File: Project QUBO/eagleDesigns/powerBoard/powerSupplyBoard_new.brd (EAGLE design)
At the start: 152.4 x 101.6 mm, 146 parts

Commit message: placed everything preliminarily
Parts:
- C15, C3, C6: value (none) -> 22 uF
- moved R39 268.9 mm to (147.3, 59.7)
- moved R40 268.2 mm to (141.0, 74.9)
- moved R38 261.8 mm to (147.3, 57.1), turned to 180 degrees
- moved R37 253.5 mm to (147.3, 62.2)
- moved REN_H 253.4 mm to (121.9, 27.9)
- moved C_OUT_5V 246.3 mm to (128.3, 7.62)
- moved R36 245.5 mm to (147.3, 64.8), turned to 180 degrees
- moved 5VCS 240.9 mm to (115.6, 36.8), turned to 270 degrees
- moved REN_T 239.0 mm to (114.3, 27.9), turned to 180 degrees
- moved R35 238.2 mm to (148.6, 72.4), turned to 180 degrees
- moved R34 230.3 mm to (148.6, 74.9)
- moved RFBT 224.5 mm to (114.3, 12.7)
- moved RFBB 214.4 mm to (114.3, 17.8)
- moved R47 214.1 mm to (147.3, 45.7)
- moved C_BYP7 205.1 mm to (123.2, 17.8)
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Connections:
- removed net N$59 (its old number): REN_B.1, REN_H.1, REN_T.2, U$5.C
- removed net N$60: R36.1, R37.2
- removed net N$61: ADC.SCL
- removed net N$63: ADC.SDA
- removed net N$75: BAT1HSOR.SHDN, HIGHSIDEMOS1.D, R48.1
- removed net N$76: ADC.CH7, R34.1, R35.2, R38.2
- removed net N$77: ADC.CH8
- removed net N$78: ADC.CH9
- removed net N$79: ADC.CH10
- removed net N$80: ADC.CH11
- removed net N$81: ADC.CH12
- removed net N$82: ADC.CH13
- removed net N$84: IOEXPANDER.23
- removed net N$86: IOEXPANDER.22
- new net N$32: ADC.CH7, R34.1, R35.2
- new net N$55: ADC.CH8, R36.1, R37.2
- net 12V: now also R42.2
- net 16V: now also R40.2
- net 3.3V: now also R46.2
- net 5V: now also R44.2
- net BAT2: now also R18.2
- net BAT3: now also R29.2, R38.2
- net GND: now also BAT1HSOR.SHDN, HIGHSIDEMOS1.D, R48.1, REN_B.1, REN_H.1, REN_T.2, U$5.C
- net N$66: now also ADC.CH9
- net N$71: now also ADC.CH10
- net N$72: now also ADC.CH11
- net N$73: now also ADC.CH12
- net N$74: now also ADC.CH13
- net SCL1: now also ADC.SCL, IOEXPANDER.22
- net SDA1: now also ADC.SDA, IOEXPANDER.23

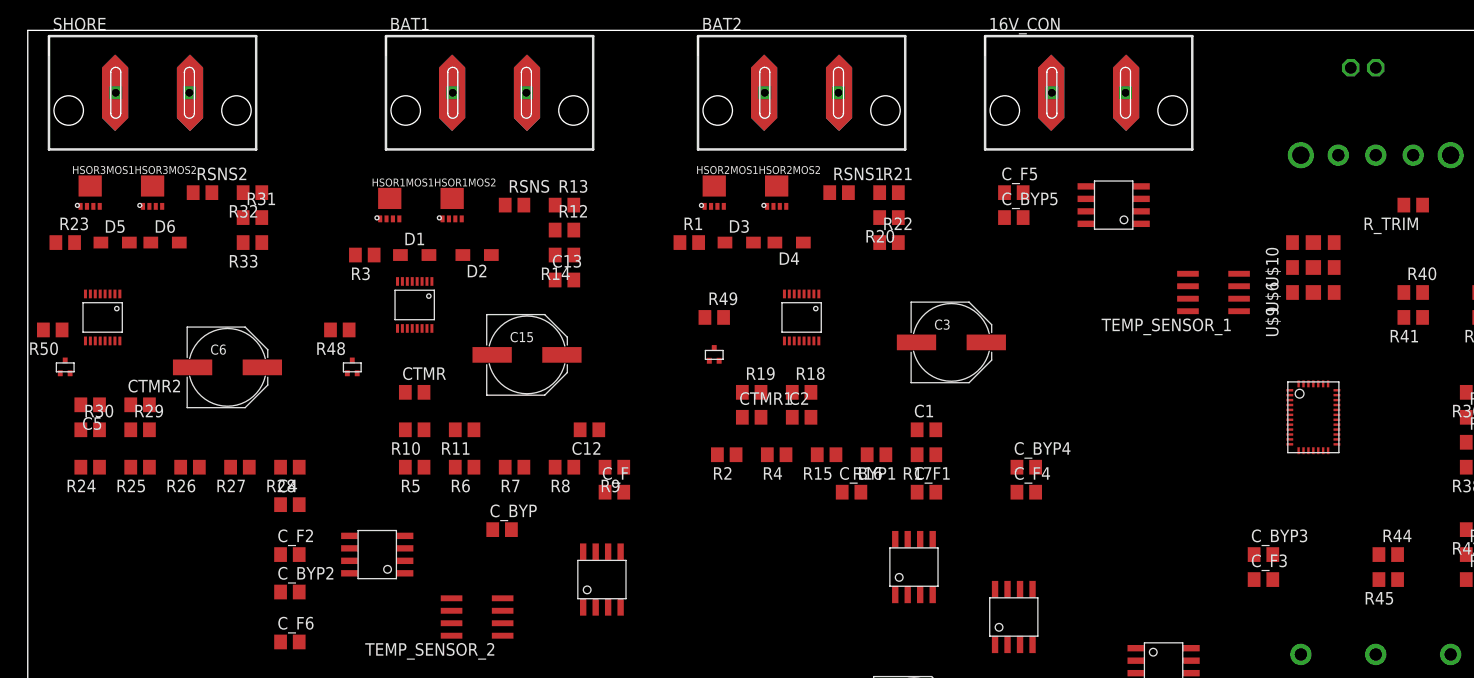
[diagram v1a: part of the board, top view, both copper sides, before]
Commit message: 
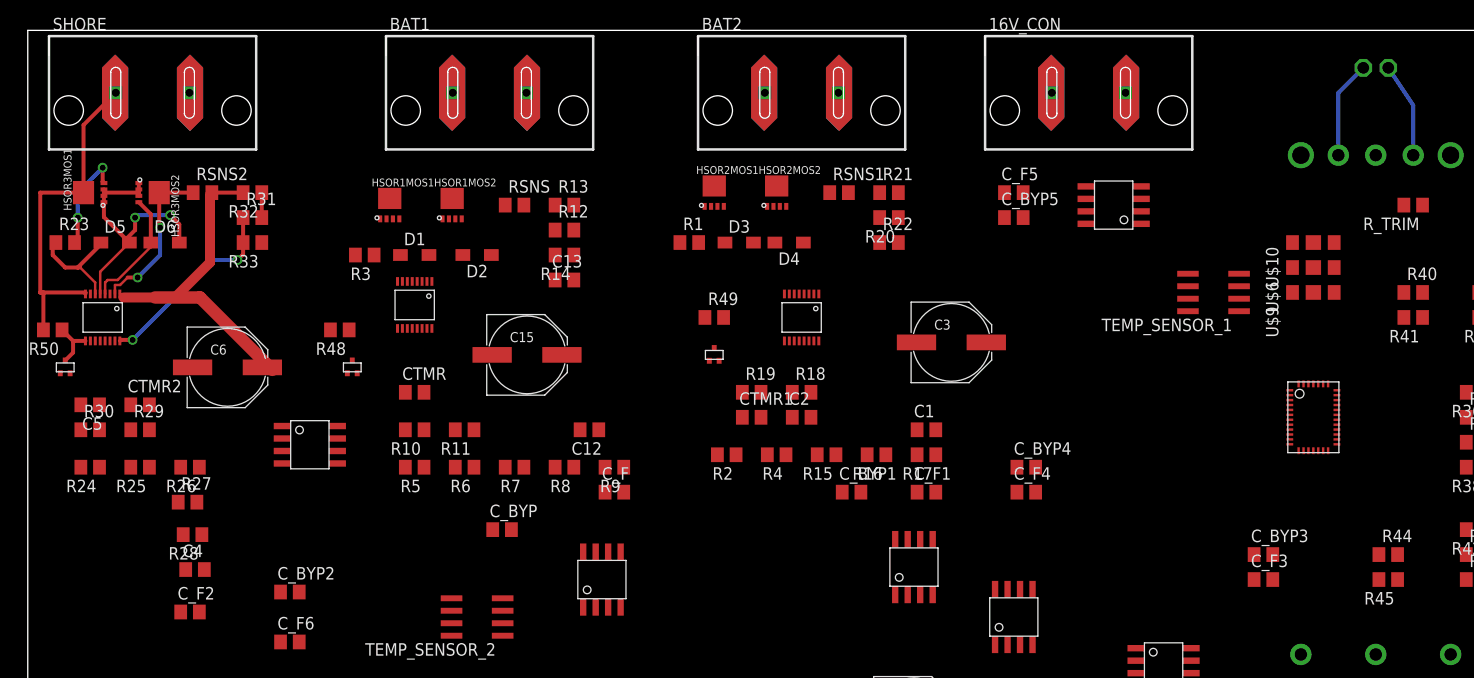
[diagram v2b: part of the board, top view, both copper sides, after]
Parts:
- moved BAT3CS 13.1 mm to (28.7, 59.4), turned to 270 degrees
- moved R28 12.0 mm to (16.8, 50.3)
- moved C_F2 11.7 mm to (16.5, 42.4)
- moved C4 11.7 mm to (17.0, 46.7)
- moved R27 6.41 mm to (16.3, 53.6), turned to 0 degrees
- moved DVL_CON 1.27 mm to (137.2, 97.8)
- turned HSOR3MOS1 to 90 degrees
- turned HSOR3MOS2 to 270 degrees
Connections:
- net N$24 renamed BAT2HSOROUT
- net N$39 renamed BAT1HSOROUT
- net N$41 renamed BAT3HSOROUT
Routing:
- net BAT3HSOROUT: track 0.00 -> 36.2 mm
- net BAT3: track 0.00 -> 35.0 mm
- net N$11: track 0.00 -> 27.2 mm, vias 0 -> 2
- net N$40: track 0.00 -> 19.9 mm, vias 0 -> 2
- net N$43: track 0.00 -> 16.6 mm, vias 0 -> 2
- net N$31: track 0.00 -> 12.4 mm
- net N$30: track 0.00 -> 11.6 mm
- net N$44: track 0.00 -> 10.6 mm, vias 0 -> 2
- net N$52: track 0.00 -> 9.94 mm
- net N$54: track 0.00 -> 9.66 mm
- net N$56: track 0.00 -> 5.17 mm
- net N$38: track 0.00 -> 2.54 mm

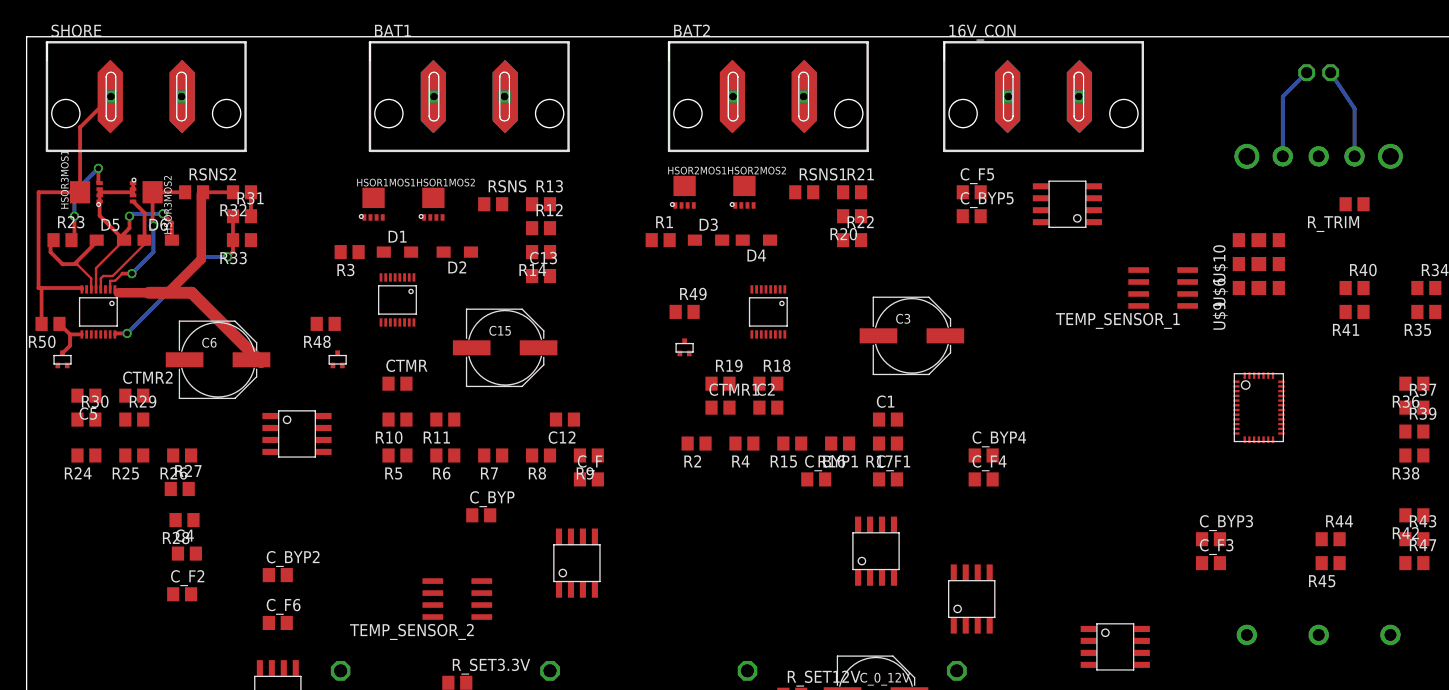
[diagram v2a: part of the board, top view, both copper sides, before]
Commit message: 
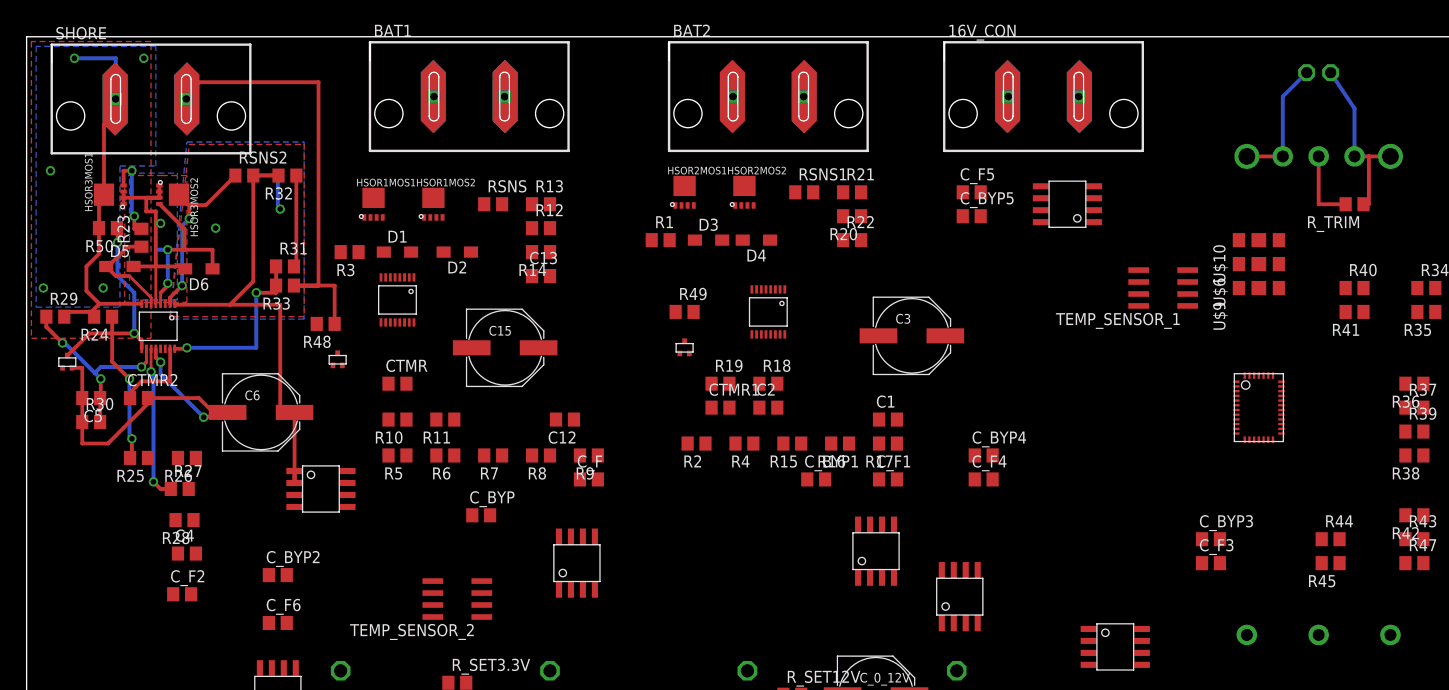
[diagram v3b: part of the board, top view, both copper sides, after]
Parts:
- moved R24 14.8 mm to (8.13, 71.9)
- moved R29 13.8 mm to (3.05, 71.9)
- moved R50 11.8 mm to (8.64, 81.3)
- moved R23 8.39 mm to (12.2, 80.3), turned to 90 degrees
- moved C6 7.22 mm to (24.9, 61.7)
- moved R31 7.03 mm to (27.4, 77.2)
- moved R33 6.65 mm to (27.4, 75.2)
- moved BAT3HSOR 6.53 mm to (14.0, 70.9)
- moved BAT3CS 6.37 mm to (31.2, 53.6)
- moved RSNS2 5.62 mm to (23.1, 86.9)
- moved D6 5.29 mm to (18.3, 77.0), turned to 180 degrees
- moved R32 5.14 mm to (27.7, 86.9)
- moved D5 2.97 mm to (9.91, 77.2)
- moved HSOR3MOS2 2.81 mm to (15.5, 84.8)
- moved HSOR3MOS1 2.55 mm to (8.89, 84.8)
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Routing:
- net GND: track 0.00 -> 85.4 mm, vias 0 -> 2
- net N$37: track 0.00 -> 21.1 mm, vias 0 -> 3
- net BAT3HSOROUT: track 36.2 -> 57.2 mm, vias 0 -> 2
- net N$56: track 5.17 -> 22.0 mm, vias 0 -> 2
- net N$36: track 0.00 -> 16.4 mm, vias 0 -> 2
- net N$33: track 0.00 -> 15.9 mm, vias 0 -> 2
- net N$54: track 9.66 -> 19.1 mm
- net N$42: track 0.00 -> 8.78 mm
- net N$62: track 0.00 -> 7.94 mm
- net BAT3: track 35.0 -> 42.5 mm, vias 0 -> 5
- net N$31: track 12.4 -> 19.8 mm, vias 0 -> 2
- net N$38: track 2.54 -> 9.91 mm
- net N$52: track 9.94 -> 13.8 mm
- net N$43: track 16.6 -> 19.1 mm
- net N$11: track 27.2 -> 25.7 mm, vias 2 -> 1
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- added copper zone on layer 1, net BAT3
- added copper zone on layer 16, net BAT3
- added copper zone on layer 1, net BAT3HSOROUT
- added copper zone on layer 16, net BAT3HSOROUT
- added copper zone on layer 1, net N$11
- added copper zone on layer 16, net N$11

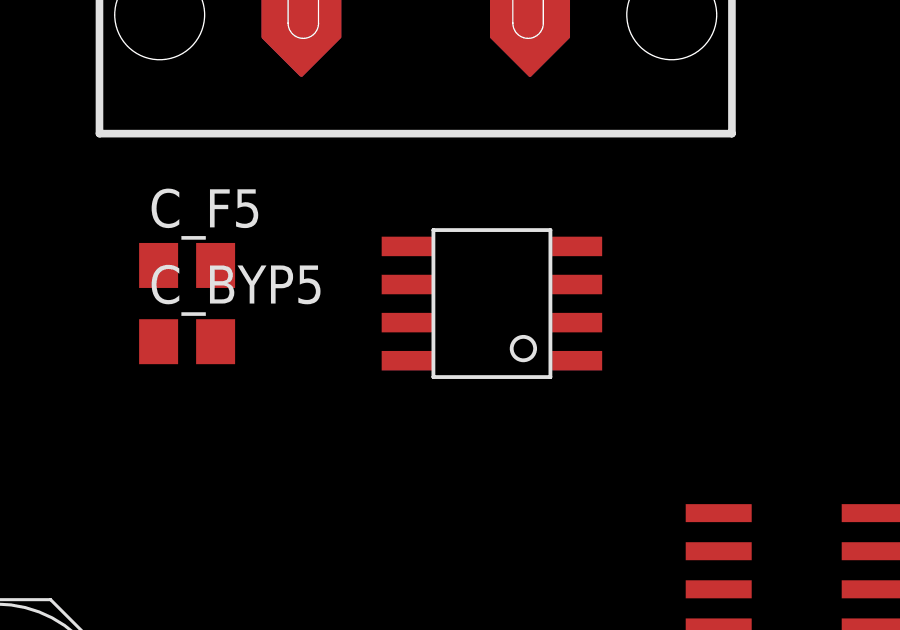
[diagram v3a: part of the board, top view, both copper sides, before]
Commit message: 
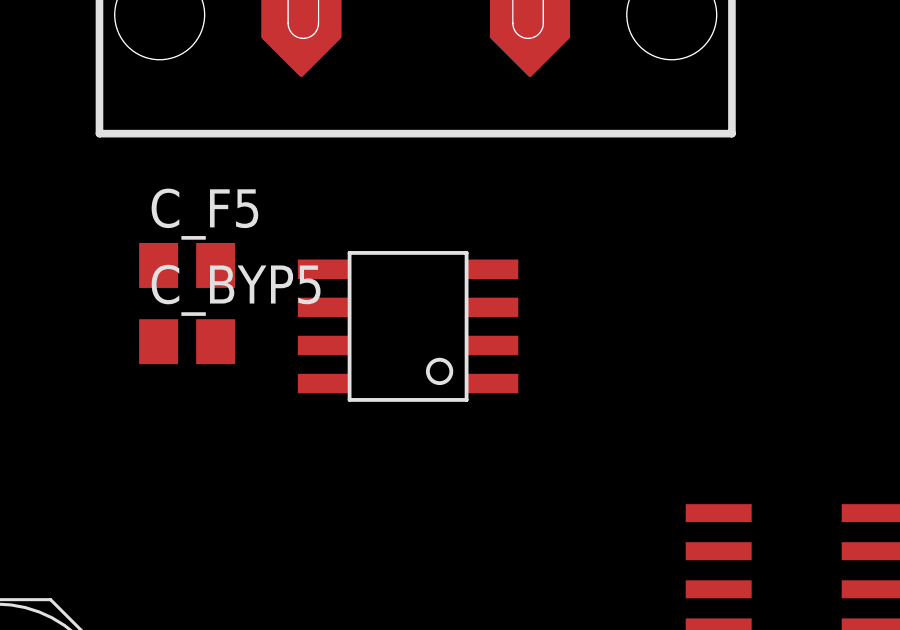
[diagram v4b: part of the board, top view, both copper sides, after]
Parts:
- moved 16VCS 2.90 mm to (107.7, 83.1)
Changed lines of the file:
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@@
 <element name="12VCS" library="allegro" package="ACS713-SOIC" value="ACS713SOIC" x="99.06" y="42.164"/>
 <element name="12VREG" library="texas" package="PTN78060W" value="PTN78060W" x="87.63" y="27.94" rot="MR0"/>
-<element name="16VCS" library="allegro" package="ACS713-SOIC" value="ACS713SOIC" x="110.49" y="83.82" rot="R90"/>
+<element name="16VCS" library="allegro" package="ACS713-SOIC" value="ACS713SOIC" x="107.696" y="83.058" rot="R90"/>
 <element name="16V_CON" library="molex" package="SUPERSABRE_2CIRCUIT" value="SUPERSABRE_2CIRCUIT" x="107.95" y="95.25"/>
 <element name="3.3VCS" library="allegro" package="ACS713-SOIC" value="ACS713SOIC" x="26.67" y="31.75"/>
@@
 <wire x1="101.28" y1="82.55" x2="86.68" y2="80.01" width="0" layer="19" extent="1-1"/>
 <wire x1="101.28" y1="85.09" x2="101.28" y2="82.55" width="0" layer="19" extent="1-1"/>
-<wire x1="107.69" y1="85.725" x2="101.28" y2="85.09" width="0" layer="19" extent="1-1"/>
-<wire x1="104.2035" y1="95.25" x2="107.69" y2="85.725" width="0" layer="19" extent="1-1"/>
+<wire x1="104.896" y1="84.963" x2="101.28" y2="85.09" width="0" layer="19" extent="1-1"/>
+<wire x1="104.2035" y1="95.25" x2="104.896" y2="84.963" width="0" layer="19" extent="1-1"/>
 <wire x1="93.93" y1="6.56" x2="108.27" y2="12.7" width="0" layer="19" extent="1-1"/>
 <wire x1="91.93" y1="6.56" x2="93.93" y2="6.56" width="0" layer="19" extent="1-1"/>
@@
 <wire x1="133.21" y1="63.98" x2="128.69" y2="74.93" width="0" layer="19" extent="1-1"/>
 <wire x1="133.21" y1="63.48" x2="133.21" y2="63.98" width="0" layer="19" extent="1-1"/>
-<wire x1="107.69" y1="81.915" x2="118.05" y2="73.025" width="0" layer="19" extent="1-1"/>
-<wire x1="99.38" y1="82.55" x2="107.69" y2="81.915" width="0" layer="19" extent="1-1"/>
+<wire x1="104.896" y1="81.153" x2="118.05" y2="73.025" width="0" layer="19" extent="1-1"/>
+<wire x1="99.38" y1="82.55" x2="104.896" y2="81.153" width="0" layer="19" extent="1-1"/>
 <wire x1="139.38" y1="48.26" x2="133.21" y2="63.48" width="0" layer="19" extent="1-1"/>
 <wire x1="124.78" y1="48.26" x2="139.38" y2="48.26" width="0" layer="19" extent="1-1"/>
@@
 <contactref element="C_IN_5V" pad="1"/>
 <contactref element="DVL_12VREG" pad="+VIN"/>
-<wire x1="113.29" y1="83.185" x2="113.29" y2="81.915" width="0" layer="19" extent="1-1"/>
-<wire x1="92.075" y1="44.19" x2="113.29" y2="81.915" width="0" layer="19" extent="1-1"/>
+<wire x1="110.496" y1="81.153" x2="110.496" y2="82.423" width="0" layer="19" extent="1-1"/>
+<wire x1="92.075" y1="44.19" x2="110.496" y2="81.153" width="0" layer="19" extent="1-1"/>
 <wire x1="90.805" y1="44.19" x2="92.075" y2="44.19" width="0" layer="19" extent="1-1"/>
 <wire x1="81.6" y1="24.13" x2="90.805" y2="44.19" width="0" layer="19" extent="1-1"/>
@@
 <vertex x="13.208" y="101.092"/>
 </polygon>
-<polygon width="0.4064" layer="16">
+<polygon width="0.4064" layer="16" rank="2">
 <vertex x="1.016" y="100.584"/>
 <vertex x="1.016" y="72.898"/>
@@
 <contactref element="16VCS" pad="P$6"/>
 <contactref element="C_F5" pad="1"/>
-<wire x1="99.38" y1="85.09" x2="107.69" y2="84.455" width="0" layer="19" extent="1-1"/>
+<wire x1="99.38" y1="85.09" x2="104.896" y2="83.693" width="0" layer="19" extent="1-1"/>
 </signal>
 <signal name="N$53">
@@
 <contactref element="16V_CON" pad="P$2"/>
 <contactref element="R40" pad="2"/>
-<wire x1="113.29" y1="84.455" x2="141.92" y2="74.93" width="0" layer="19" extent="1-1"/>
-<wire x1="113.29" y1="85.725" x2="113.29" y2="84.455" width="0" layer="19" extent="1-1"/>
-<wire x1="111.6965" y1="95.25" x2="113.29" y2="85.725" width="0" layer="19" extent="1-1"/>
+<wire x1="110.496" y1="83.693" x2="141.92" y2="74.93" width="0" layer="19" extent="1-1"/>
+<wire x1="110.496" y1="84.963" x2="110.496" y2="83.693" width="0" layer="19" extent="1-1"/>
+<wire x1="111.6965" y1="95.25" x2="110.496" y2="84.963" width="0" layer="19" extent="1-1"/>
 </signal>
 <signal name="12V">
@@
 <contactref element="16VCS" pad="P$7"/>
 <contactref element="ADC" pad="CH3"/>
-<wire x1="128.41" y1="59.98" x2="107.69" y2="83.185" width="0" layer="19" extent="1-1"/>
+<wire x1="128.41" y1="59.98" x2="104.896" y2="82.423" width="0" layer="19" extent="1-1"/>
 </signal>
 <signal name="12CSOUT">
